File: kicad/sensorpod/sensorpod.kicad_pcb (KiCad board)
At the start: 2 copper layers, 49.3 x 68.3 mm, 43 parts, among them P1 HEADER_(8_WAY)

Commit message: Minor tweaks
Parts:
- moved SR1 5.99 mm to (208.9, 153.0)
- moved R1 4.96 mm to (212.7, 146.1)
- moved R2 4.96 mm to (210.2, 146.1)
- moved R4 4.96 mm to (205.1, 146.1)
- moved R3 4.96 mm to (207.6, 146.1)
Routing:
- net N-0000011: track 60.6 -> 67.0 mm
- net N-0000025: track 92.5 -> 98.9 mm
- net N-000001: track 47.1 -> 53.5 mm
- net N-0000026: track 77.1 -> 83.5 mm
- net N-0000020: track 28.5 -> 24.4 mm
- net +5V: track 317.2 -> 320.0 mm
- net N-0000022: track 26.4 -> 23.6 mm
- net N-0000019: track 42.1 -> 40.5 mm
- net N-0000017: track 4.67 -> 3.40 mm
- net N-0000015: track 4.67 -> 3.40 mm
- net N-0000018: track 5.19 -> 3.92 mm
- net N-0000016: track 5.19 -> 3.92 mm
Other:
- board size 49.3 x 68.3 mm -> 46 x 71 mm
- board text added: "©2016 Oak House Technology"

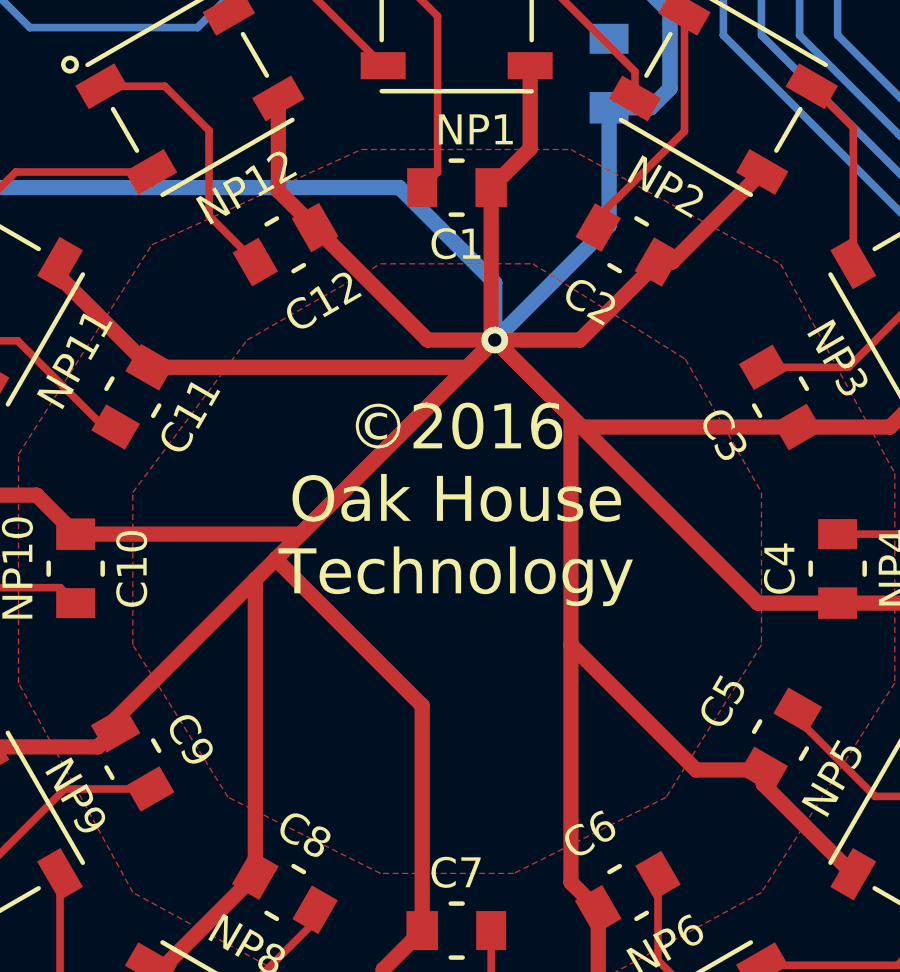
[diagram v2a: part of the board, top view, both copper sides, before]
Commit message: Added extra vias to central 5V fill
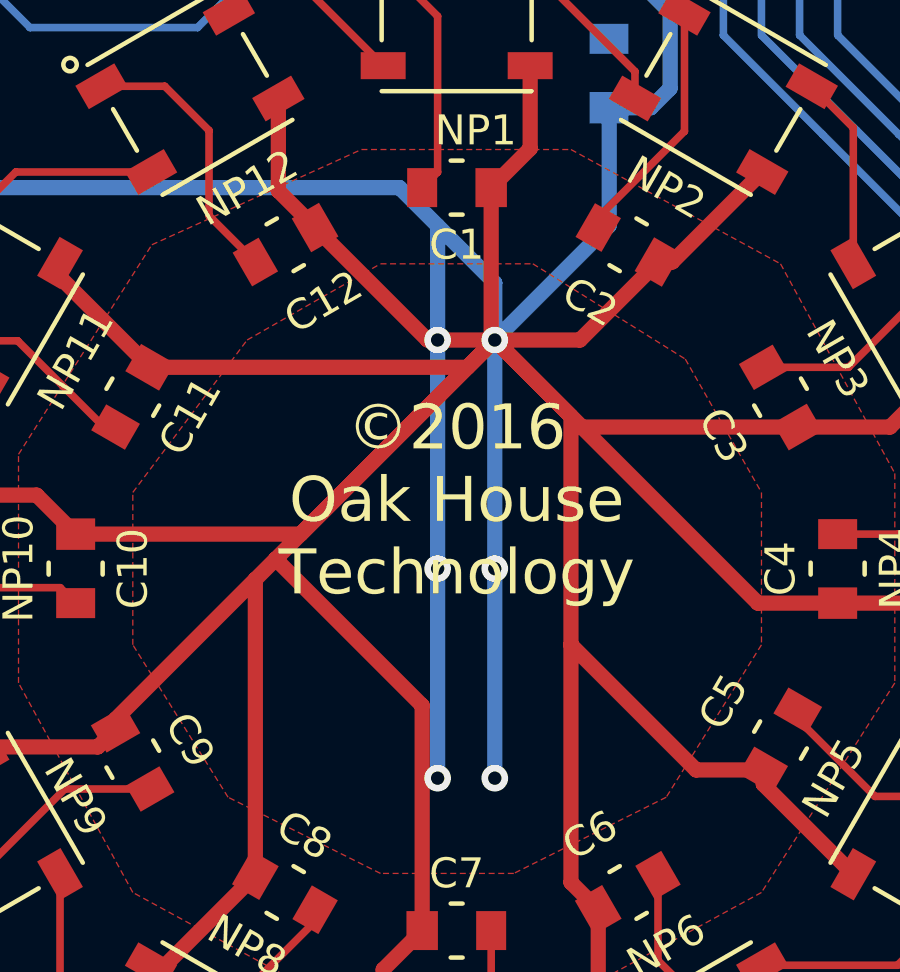
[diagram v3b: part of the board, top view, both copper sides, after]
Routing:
- net +5V: track 320.0 -> 353.0 mm, vias 1 -> 6
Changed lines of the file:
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@@
     (thickness 1.6)
     (drawings 13)
-    (tracks 210)
+    (tracks 222)
     (zones 0)
     (modules 43)
@@
   (gr_line (start 221.12 198.03) (end 221.12 155.03) (angle 90) (layer Edge.Cuts) (width 0.1))
   (gr_line (start 189.12 212.03) (end 207.12 212.03) (angle 90) (layer Edge.Cuts) (width 0.1))
+  (segment (start 197.485 183.515) (end 197.485 176.53) (width 0.508) (layer B.Cu) (net 1))
+  (via (at 197.485 176.53) (size 0.889) (layers F.Cu B.Cu) (net 1))
+  (segment (start 197.485 176.53) (end 197.485 168.91) (width 0.508) (layer B.Cu) (net 1))
+  (via (at 197.485 183.515) (size 0.889) (layers F.Cu B.Cu) (net 1))
+  (segment (start 197.485 165.1) (end 197.485 168.91) (width 0.508) (layer B.Cu) (net 1))
+  (via (at 197.485 168.91) (size 0.889) (layers F.Cu B.Cu) (net 1))
+  (segment (start 199.39 183.515) (end 199.39 176.53) (width 0.508) (layer B.Cu) (net 1))
+  (via (at 199.39 176.53) (size 0.889) (layers F.Cu B.Cu) (net 1))
+  (segment (start 199.39 176.53) (end 199.39 168.91) (width 0.508) (layer B.Cu) (net 1))
+  (via (at 199.39 183.515) (size 0.889) (layers F.Cu B.Cu) (net 1))
   (segment (start 204.47 155.735) (end 204.47 157.226) (width 0.508) (layer B.Cu) (net 1))
   (segment (start 204.59 161.17) (end 203.2 161.17) (width 0.508) (layer B.Cu) (net 1))
@@
   (segment (start 203.2 165.1) (end 199.39 168.91) (width 0.508) (layer B.Cu) (net 1))
   (segment (start 199.39 168.91) (end 199.39 167.005) (width 0.508) (layer B.Cu) (net 1))
-  (segment (start 199.39 167.005) (end 196.215 163.83) (width 0.508) (layer B.Cu) (net 1))
+  (segment (start 199.39 167.005) (end 197.485 165.1) (width 0.508) (layer B.Cu) (net 1))
+  (segment (start 197.485 165.1) (end 196.215 163.83) (width 0.508) (layer B.Cu) (net 1))
   (segment (start 192.176762 160.858942) (end 192.176762 163.935833) (width 0.508) (layer F.Cu) (net 1))
   (segment (start 192.176762 163.935833) (end 193.400929 165.16) (width 0.508) (layer F.Cu) (net 1))
@@
   (segment (start 199.39 168.91) (end 202.230929 168.91) (width 0.508) (layer F.Cu) (net 1))
   (segment (start 202.230929 168.91) (end 204.830929 166.31) (width 0.508) (layer F.Cu) (net 1))
-  (segment (start 199.39 168.91) (end 197.150929 168.91) (width 0.508) (layer F.Cu) (net 1))
+  (segment (start 199.39 168.91) (end 197.485 168.91) (width 0.508) (layer F.Cu) (net 1))
+  (segment (start 197.485 168.91) (end 197.150929 168.91) (width 0.508) (layer F.Cu) (net 1))
   (segment (start 197.150929 168.91) (end 193.400929 165.16) (width 0.508) (layer F.Cu) (net 1))
   (segment (start 199.27 163.83) (end 199.27 168.79) (width 0.508) (layer F.Cu) (net 1))

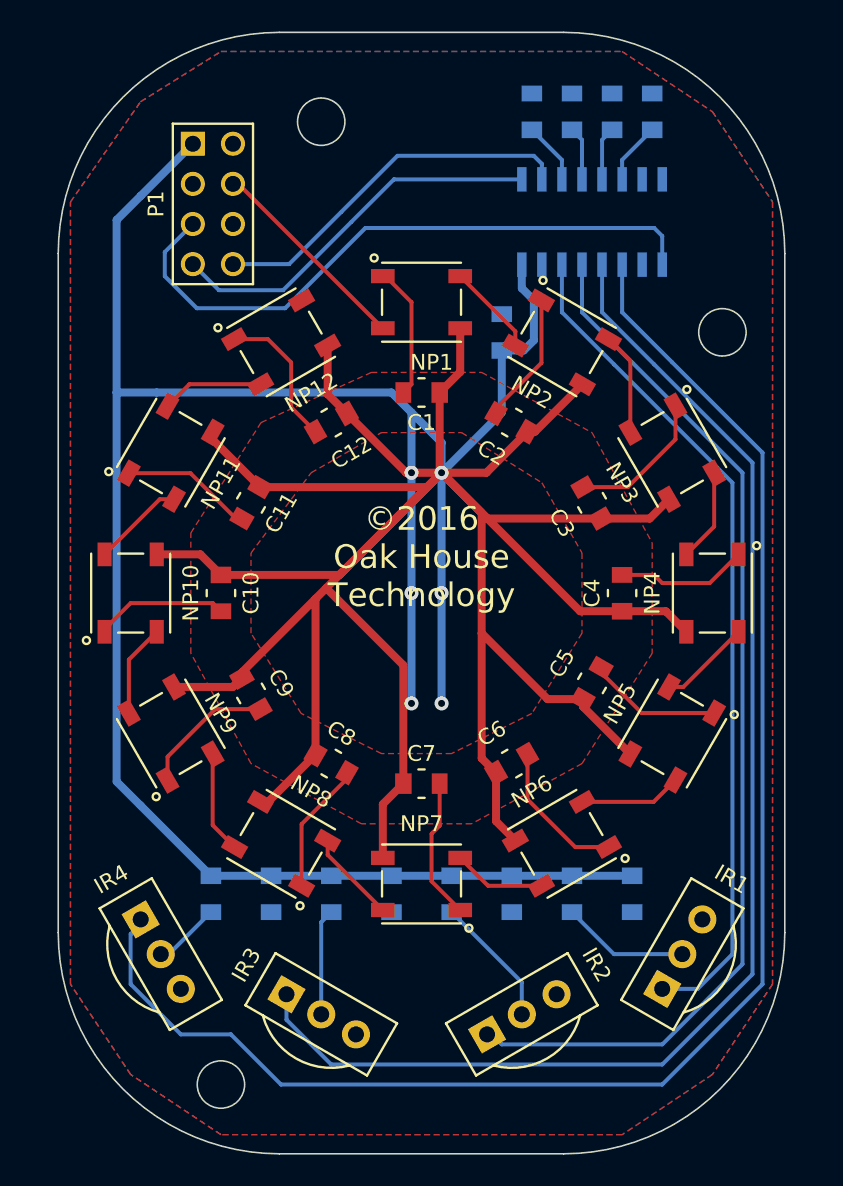
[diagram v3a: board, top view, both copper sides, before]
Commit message: Corrected wrong pad assignment on ir receiver footprint
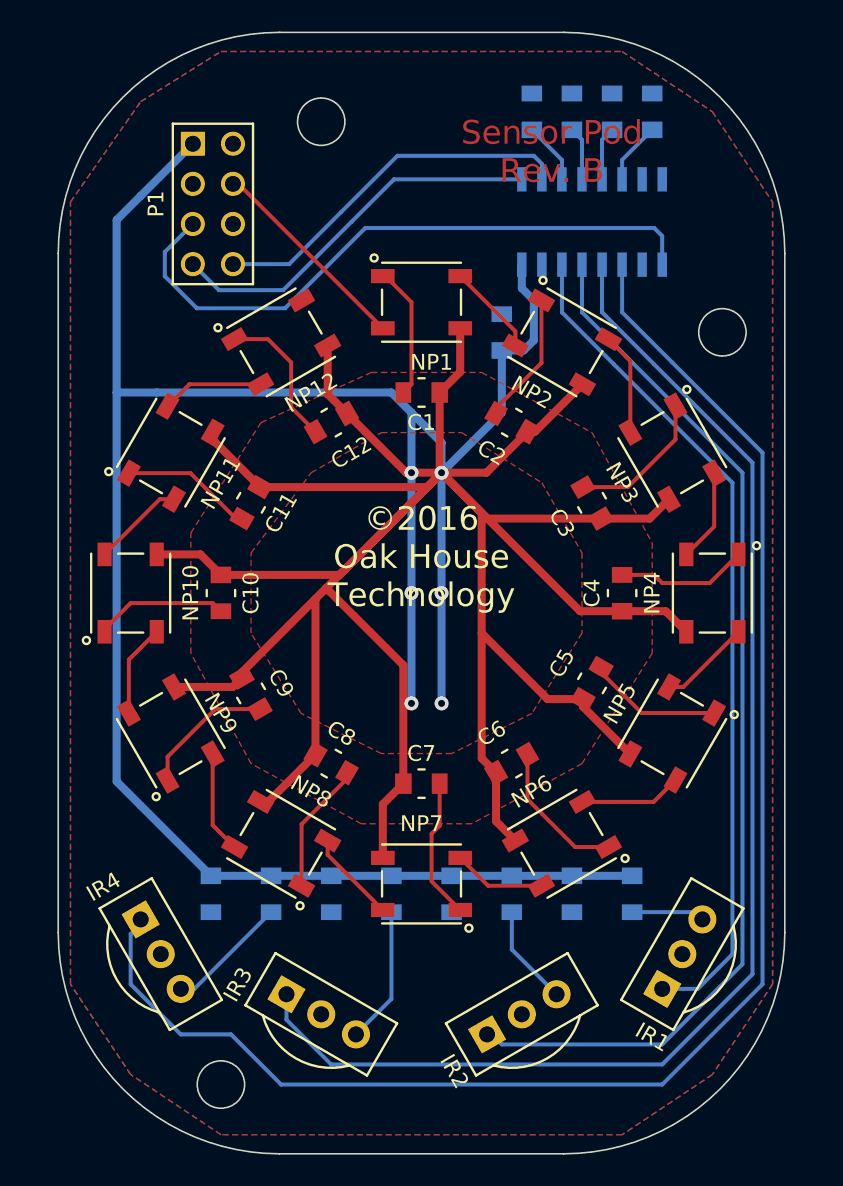
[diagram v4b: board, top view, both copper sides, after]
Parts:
- moved C27 3.81 mm to (184.8, 195.6)
- moved C28 3.81 mm to (192.4, 195.6)
- moved C29 3.81 mm to (200.0, 195.6)
- moved C30 3.81 mm to (207.6, 195.6)
- moved R10 3.81 mm to (203.8, 195.6)
- moved R11 3.81 mm to (196.2, 195.6)
- moved R12 3.81 mm to (188.6, 195.6)
- moved R9 3.81 mm to (211.5, 195.6)
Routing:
- net N-0000030: track 4.28 -> 7.73 mm
- net N-0000031: track 8.09 -> 4.64 mm
- net N-0000029: track 6.73 -> 8.67 mm
- net N-0000028: track 8.31 -> 6.37 mm
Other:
- board text added: "Sensor Pod Rev. B"

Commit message: Put in alternate IR receiver locations on sensor pod
Should make things easier when the pins need to be bent to lie them
flat on the chest/back pods
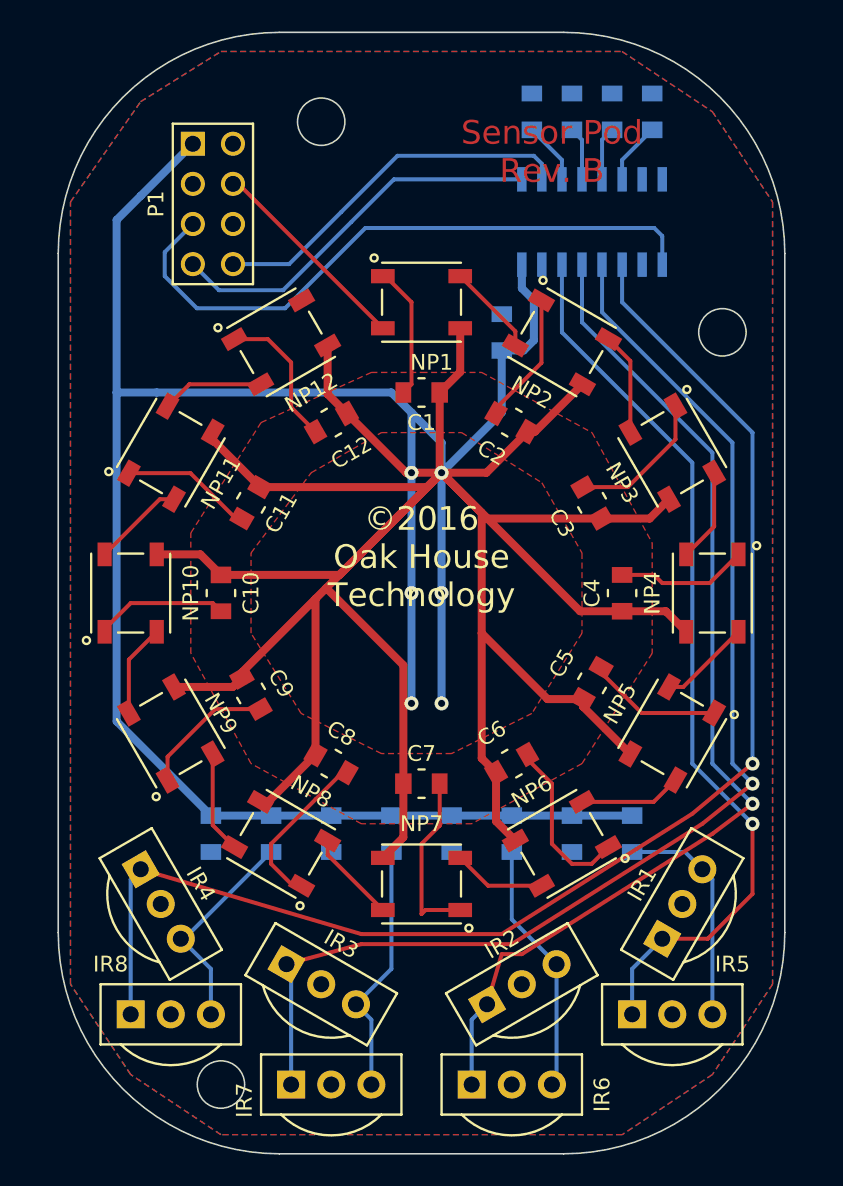
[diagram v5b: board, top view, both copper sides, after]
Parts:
- added IR5: TSOP38438, Minicast, F.Cu at (214.0, 203.2)
- added IR6: TSOP38438, Minicast, F.Cu at (203.8, 207.6)
- added IR7: TSOP38438, Minicast, F.Cu at (192.4, 207.6)
- added IR8: TSOP38438, Minicast, F.Cu at (182.2, 203.2)
- moved C27 3.81 mm to (184.8, 191.8)
- moved C28 3.81 mm to (192.4, 191.8)
- moved C29 3.81 mm to (200.0, 191.8)
- moved C30 3.81 mm to (207.6, 191.8)
- moved R10 3.81 mm to (203.8, 191.8)
- moved R11 3.81 mm to (196.2, 191.8)
- moved R12 3.81 mm to (188.6, 191.8)
- moved R9 3.81 mm to (211.5, 191.8)
- moved IR1 3.17 mm to (214.6, 196.2)
- moved IR4 3.17 mm to (181.6, 196.2)
- moved IR2 1.91 mm to (204.5, 201.3)
- moved IR3 1.91 mm to (191.8, 201.3)
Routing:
- net N-0000010: track 98.9 -> 87.1 mm, vias 0 -> 1
- net N-000009: track 4.64 -> 14.3 mm
- net N-000005: track 6.37 -> 16.0 mm
- net N-000008: track 8.67 -> 16.1 mm
- net N-0000011: track 83.5 -> 77.3 mm, vias 0 -> 1
- net GND: track 104.0 -> 110.0 mm
- net N-000007: track 7.73 -> 13.6 mm
- net N-000006: track 53.5 -> 57.3 mm, vias 0 -> 1
- net +5V: track 353.0 -> 349.2 mm
- net N-0000013: track 67.0 -> 66.1 mm, vias 0 -> 1
